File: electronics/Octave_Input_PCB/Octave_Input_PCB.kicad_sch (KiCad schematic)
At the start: 58 parts, among them J1 HRO_TYPE-C-31-M-12, SW1 SW_Hot_Swap_Socket, SW10 SW_Hot_Swap_Socket, SW11 SW_Hot_Swap_Socket, SW12 SW_Hot_Swap_Socket, SW13 SW_Hot_Swap_Socket, SW14 Alps_Alpine_RKJXV1224, SW15 Bourns_PEC12R-4xxxF-Sxxx, SW2 SW_Hot_Swap_Socket, SW3 SW_Hot_Swap_Socket, SW4 SW_Hot_Swap_Socket, SW5 SW_Hot_Swap_Socket, SW6 SW_Hot_Swap_Socket, SW7 SW_Hot_Swap_Socket, SW8 SW_Hot_Swap_Socket, SW9 SW_Hot_Swap_Socket, U1 AP2112K-3.3, U2 Raspberry_Pi_RP2040, U3 W25Q64JVSS

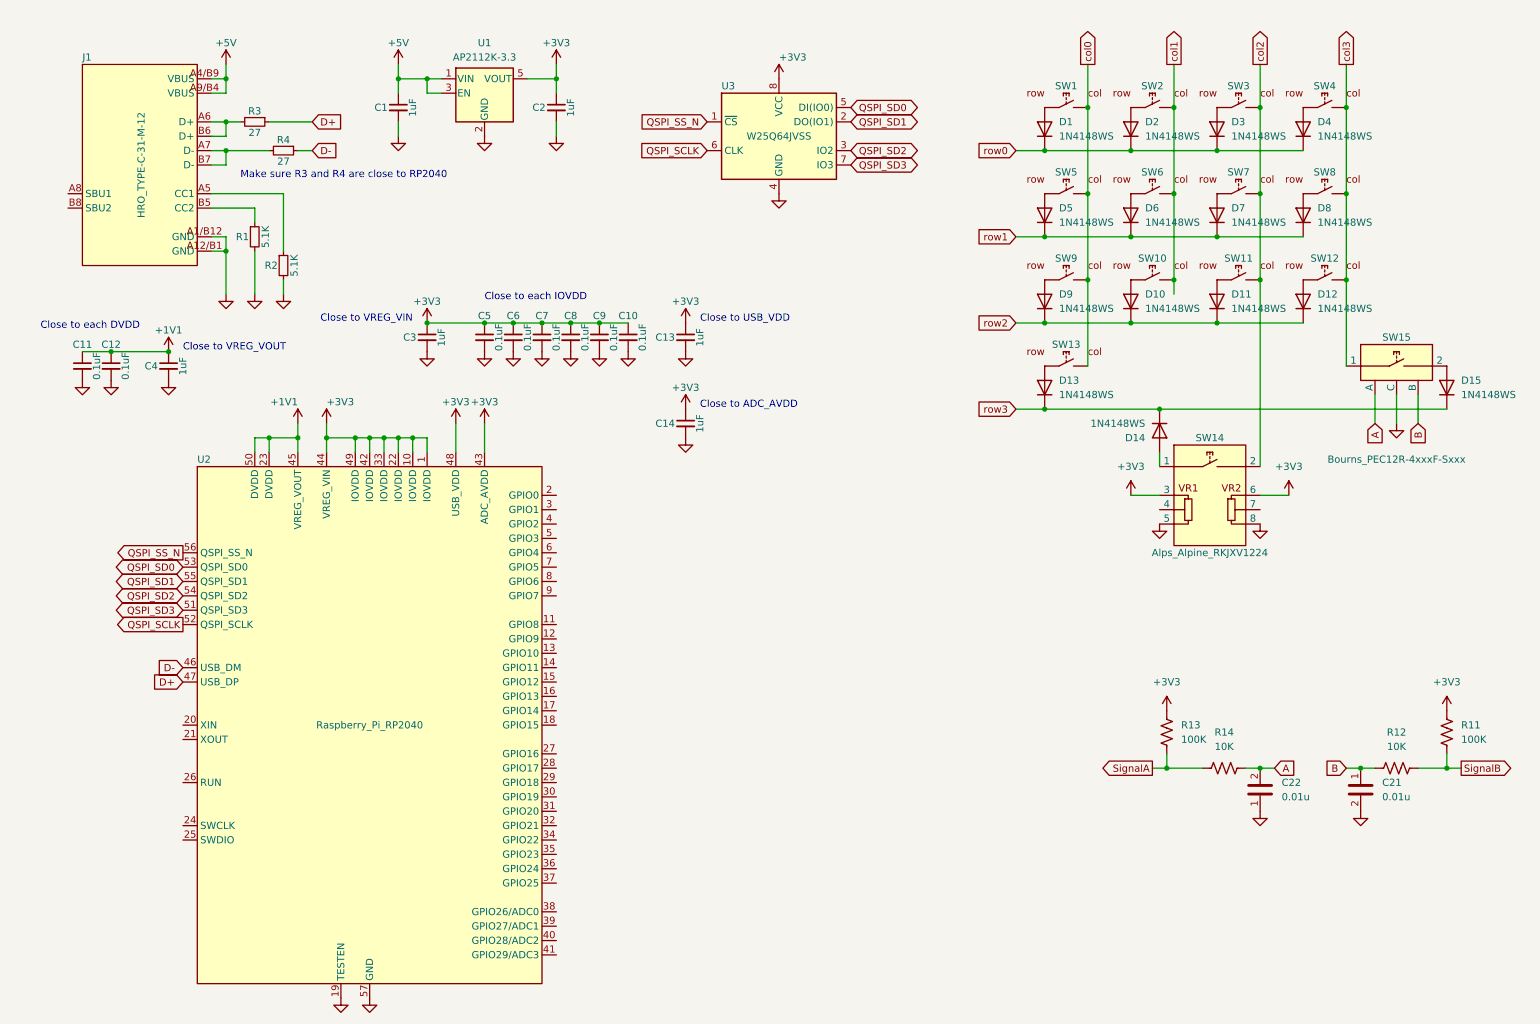
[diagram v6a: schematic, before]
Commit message: Add crystal resonator
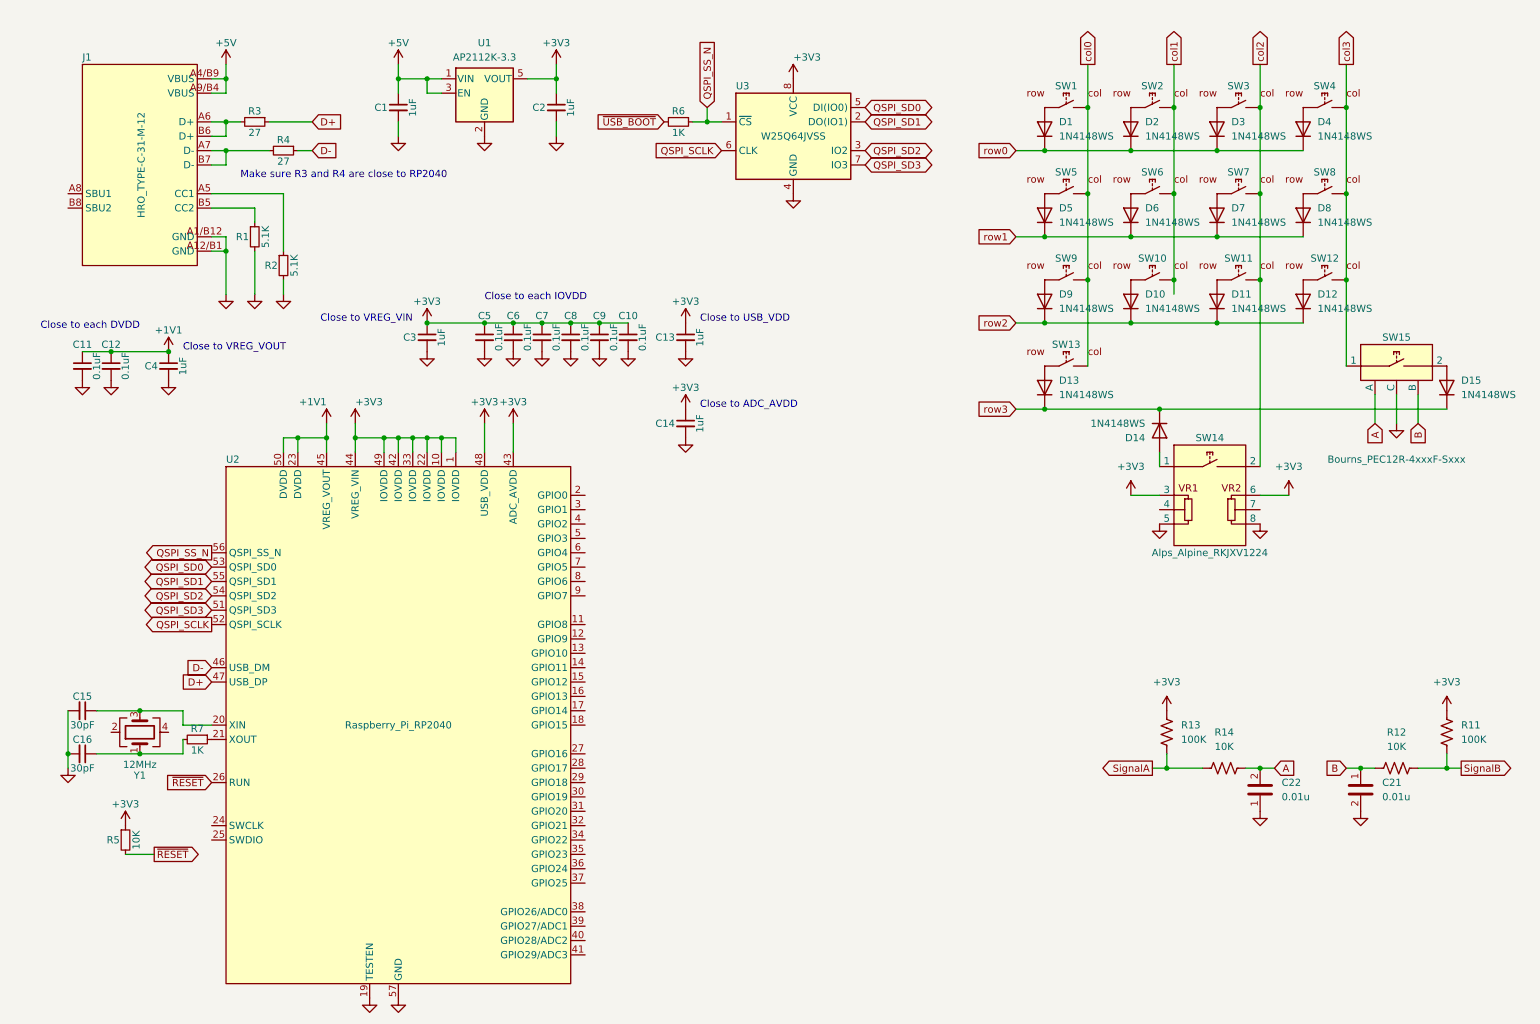
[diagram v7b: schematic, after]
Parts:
- added C15, C16: 30pF, Capacitor_SMD:C_0402_1005Metric, symbol Device:C_Small
- added R5: 10K, Resistor_SMD:R_0402_1005Metric, symbol Device:R_Small
- added R6, R7: 1K, Resistor_SMD:R_0402_1005Metric, symbol Device:R_Small
- added Y1: 12MHz, Crystal:Crystal_SMD_3225-4Pin_3.2x2.5mm, symbol Device:Crystal_GND24
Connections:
- net +3V3: now also R5.1
- net GND: now also C15.2, C16.2
- net QSPI_SS_N: now also R6.1
- net at U2.20 (XIN): now also C15.1, Y1.3
- net at U2.21 (XOUT): now also R7.1
- net ~{RESET}: now reaches U2.26 (RUN)
- net ~{RESET}: now also R5.2
- new net: C16.1, R7.2, Y1.1
- new net ~{USB_BOOT}: R6.2
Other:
- moved on the sheet: U2, U3

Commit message: [WIP] Update schematic and PCB
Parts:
- added SW21, SW22: Alps_Alpine_SKRP, Octave_Library:Tactile_Switch_SKRP_ Series, symbol Octave_Library:Alps_Alpine_SKRP
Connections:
- net GND: now also SW21.1, SW21.3, SW22.1, SW22.3
- net ~{RESET}: now also SW21.2, SW21.4
- net ~{USB_BOOT}: now also SW22.2, SW22.4
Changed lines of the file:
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@@
   (title_block
     (title "Octave - Input PCB")
-    (date "2022-05-08")
+    (date "2022-05-21")
     (rev "5.a")
     (comment 4 "https://github.com/takayoshiotake/octave-12-key-macropad")
@@
   (junction (at 233.68 149.86) (diameter 0) (color 0 0 0 0)
   )
+  (junction (at 33.02 175.26) (diameter 0) (color 0 0 0 0)
+  )
   (junction (at 116.84 71.12) (diameter 0) (color 0 0 0 0)
   )
@@
   (junction (at 195.58 40.64) (diameter 0) (color 0 0 0 0)
   )
+  (junction (at 120.65 53.34) (diameter 0) (color 0 0 0 0)
+  )
   (junction (at 233.68 48.26) (diameter 0) (color 0 0 0 0)
   )
@@
   (junction (at 251.46 149.86) (diameter 0) (color 0 0 0 0)
   )
+  (junction (at 33.02 167.64) (diameter 0) (color 0 0 0 0)
+  )
   (junction (at 233.68 63.5) (diameter 0) (color 0 0 0 0)
   )
@@
   (junction (at 248.92 48.26) (diameter 0) (color 0 0 0 0)
   )
+  (junction (at 33.02 165.1) (diameter 0) (color 0 0 0 0)
+  )
   (junction (at 210.82 40.64) (diameter 0) (color 0 0 0 0)
   )
   (junction (at 73.66 91.44) (diameter 0) (color 0 0 0 0)
   )
+  (junction (at 123.19 45.72) (diameter 0) (color 0 0 0 0)
+  )
   (junction (at 30.48 76.2) (diameter 0) (color 0 0 0 0)
   )
@@
     (stroke (width 0) (type default) (color 0 0 0 0))
   )
+  (wire (pts (xy 118.11 45.72) (xy 123.19 45.72))
+    (stroke (width 0) (type default) (color 0 0 0 0))
+  )
   (wire (pts (xy 48.26 38.1) (xy 50.8 38.1))
     (stroke (width 0) (type default) (color 0 0 0 0))
@@
     (stroke (width 0) (type default) (color 0 0 0 0))
   )
+  (wire (pts (xy 120.65 53.34) (xy 123.19 53.34))
+    (stroke (width 0) (type default) (color 0 0 0 0))
+  )
   (wire (pts (xy 203.2 33.02) (xy 203.2 48.26))
     (stroke (width 0) (type default) (color 0 0 0 0))
@@
     (stroke (width 0) (type default) (color 0 0 0 0))
   )
+  (wire (pts (xy 33.02 165.1) (xy 33.02 167.64))
+    (stroke (width 0) (type default) (color 0 0 0 0))
+  )
   (wire (pts (xy 50.8 25.4) (xy 50.8 27.94))
     (stroke (width 0) (type default) (color 0 0 0 0))
@@
     (stroke (width 0) (type default) (color 0 0 0 0))
   )
+  (wire (pts (xy 123.19 45.72) (xy 125.73 45.72))
+    (stroke (width 0) (type default) (color 0 0 0 0))
+  )
   (wire (pts (xy 248.92 48.26) (xy 248.92 63.5))
     (stroke (width 0) (type default) (color 0 0 0 0))
@@
     (stroke (width 0) (type default) (color 0 0 0 0))
   )
+  (wire (pts (xy 30.48 175.26) (xy 33.02 175.26))
+    (stroke (width 0) (type default) (color 0 0 0 0))
+  )
   (wire (pts (xy 233.68 48.26) (xy 233.68 63.5))
     (stroke (width 0) (type default) (color 0 0 0 0))
   )
+  (wire (pts (xy 30.48 167.64) (xy 33.02 167.64))
+    (stroke (width 0) (type default) (color 0 0 0 0))
+  )
   (wire (pts (xy 88.9 91.44) (xy 86.36 91.44))
     (stroke (width 0) (type default) (color 0 0 0 0))
@@
     (stroke (width 0) (type default) (color 0 0 0 0))
   )
+  (wire (pts (xy 118.11 53.34) (xy 120.65 53.34))
+    (stroke (width 0) (type default) (color 0 0 0 0))
+  )
   (wire (pts (xy 48.26 30.48) (xy 50.8 30.48))
     (stroke (width 0) (type default) (color 0 0 0 0))
@@
   )
   (wire (pts (xy 203.2 63.5) (xy 203.2 78.74))
+    (stroke (width 0) (type default) (color 0 0 0 0))
+  )
+  (wire (pts (xy 33.02 175.26) (xy 35.56 175.26))
+    (stroke (width 0) (type default) (color 0 0 0 0))
+  )
+  (wire (pts (xy 33.02 167.64) (xy 35.56 167.64))
     (stroke (width 0) (type default) (color 0 0 0 0))
   )
@@
     )
   )
+  (global_label "~{USB_BOOT}" (shape output) (at 125.73 45.72 0) (fields_autoplaced)
+    (effects (font (size 1.27 1.27)) (justify left))
+    (property "Intersheet References" "${INTERSHEET_REFS}" (id 0) (at 137.8193 45.6406 0)
+      (effects (font (size 1.27 1.27)) (justify left) hide)
+    )
+  )
   (global_label "A" (shape input) (at 254 88.9 270) (fields_autoplaced)
     (effects (font (size 1.27 1.27)) (justify right))
@@
     (pin "1")
     (pin "2")
+  )
+  (symbol (lib_id "Octave_Library:Alps_Alpine_SKRP") (at 33.02 171.45 90) (unit 1)
+    (in_bom yes) (on_board yes)
+    (property "Reference" "SW21" (id 0) (at 36.195 171.45 90)
+      (effects (font (size 1.27 1.27)) (justify right))
+    )
+    (property "Value" "Alps_Alpine_SKRP" (id 1) (at 36.83 172.0849 90)
+      (effects (font (size 1.27 1.27)) (justify right) hide)
+    )
+    (property "Footprint" "Octave_Library:Tactile_Switch_SKRP_ Series" (id 2) (at 38.1 171.45 0)
+      (effects (font (size 1.27 1.27)) hide)
+    )
+    (property "Datasheet" "" (id 3) (at 27.94 171.45 0)
+      (effects (font (size 1.27 1.27)) hide)
+    )
+    (pin "1")
+    (pin "2")
+    (pin "3")
+    (pin "4")
   )
   (symbol (lib_id "Device:R_Small") (at 130.81 35.56 270) (unit 1)
@@
     (pin "2")
   )
+  (symbol (lib_id "Octave_Library:Alps_Alpine_SKRP") (at 120.65 49.53 90) (unit 1)
+    (in_bom yes) (on_board yes)
+    (property "Reference" "SW22" (id 0) (at 123.825 49.53 90)
+      (effects (font (size 1.27 1.27)) (justify right))
+    )
+    (property "Value" "Alps_Alpine_SKRP" (id 1) (at 124.46 50.1649 90)
+      (effects (font (size 1.27 1.27)) (justify right) hide)
+    )
+    (property "Footprint" "Octave_Library:Tactile_Switch_SKRP_ Series" (id 2) (at 125.73 49.53 0)
+      (effects (font (size 1.27 1.27)) hide)
+    )
+    (property "Datasheet" "" (id 3) (at 115.57 49.53 0)
+      (effects (font (size 1.27 1.27)) hide)
+    )
+    (pin "1")
+    (pin "2")
+    (pin "3")
+    (pin "4")
+  )
   (symbol (lib_id "power:+3V3") (at 132.08 86.36 0) (unit 1)
     (in_bom yes) (on_board yes)
@@
     )
     (property "Datasheet" "" (id 3) (at 55.88 66.04 0)
+      (effects (font (size 1.27 1.27)) hide)
+    )
+    (pin "1")
+  )
+  (symbol (lib_id "power:GND") (at 120.65 53.34 0) (unit 1)
+    (in_bom yes) (on_board yes) (fields_autoplaced)
+    (property "Reference" "#PWR?" (id 0) (at 120.65 59.69 0)
+      (effects (font (size 1.27 1.27)) hide)
+    )
+    (property "Value" "GND" (id 1) (at 120.65 58.42 0)
+      (effects (font (size 1.27 1.27)) hide)
+    )
+    (property "Footprint" "" (id 2) (at 120.65 53.34 0)
+      (effects (font (size 1.27 1.27)) hide)
+    )
+    (property "Datasheet" "" (id 3) (at 120.65 53.34 0)
       (effects (font (size 1.27 1.27)) hide)
     )
@@
     (pin "1")
   )
+  (symbol (lib_id "power:GND") (at 33.02 175.26 0) (unit 1)
+    (in_bom yes) (on_board yes) (fields_autoplaced)
+    (property "Reference" "#PWR0142" (id 0) (at 33.02 181.61 0)
+      (effects (font (size 1.27 1.27)) hide)
+    )
+    (property "Value" "GND" (id 1) (at 33.02 180.34 0)
+      (effects (font (size 1.27 1.27)) hide)
+    )
+    (property "Footprint" "" (id 2) (at 33.02 175.26 0)
+      (effects (font (size 1.27 1.27)) hide)
+    )
+    (property "Datasheet" "" (id 3) (at 33.02 175.26 0)
+      (effects (font (size 1.27 1.27)) hide)
+    )
+    (pin "1")
+  )
   (symbol (lib_id "power:GND") (at 76.2 190.5 0) (unit 1)
     (in_bom yes) (on_board yes) (fields_autoplaced)
@@
       (reference "#PWR0141") (unit 1) (value "+3V3") (footprint "")
     )
+    (path "/ddb1239c-d7de-4856-bf69-989ec25f073c"
+      (reference "#PWR0142") (unit 1) (value "GND") (footprint "")
+    )
+    (path "/52d5fd6e-adb9-4662-8217-2b0ebb6c2141"
+      (reference "#PWR?") (unit 1) (value "GND") (footprint "")
+    )
     (path "/b4a74826-80b4-490c-898e-4ec787ca4628"
       (reference "C1") (unit 1) (value "1uF") (footprint "Capacitor_SMD:C_0402_1005Metric")
@@
       (reference "SW15") (unit 1) (value "Bourns_PEC12R-4xxxF-Sxxx") (footprint "Octave_Library:Incremental_Encoder_PEC12R-4xxxF-Sxxxx")
     )
+    (path "/130f44fe-e527-4bcc-86bb-5f52ac0ca6b7"
+      (reference "SW21") (unit 1) (value "Alps_Alpine_SKRP") (footprint "Octave_Library:Tactile_Switch_SKRP_ Series")
+    )
+    (path "/4dae5535-a9c3-4172-8f7d-fac9a279b13a"
+      (reference "SW22") (unit 1) (value "Alps_Alpine_SKRP") (footprint "Octave_Library:Tactile_Switch_SKRP_ Series")
+    )
     (path "/da6cca14-5ee3-4c97-bb6d-c82322b5e230"
